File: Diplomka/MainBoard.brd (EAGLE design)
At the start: 100 x 80 mm, 6 parts, among them K1 ARK550/2, K2 ARK550/2, U1 ESP32-WROOM-32, U2 AMS1117-3.3

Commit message: Hotová první verze schématu
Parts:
- added LED1: (no value), led:CHIP-LED0805
- added Q1: AP2012P3C-P22, SamacSys_Parts:AP2012P3CP22
- added Q2: BC817-40LT1SMD, transistor-npn:SOT23-BEC
- added R1, R4: 1K, rcl:R0805
- added R10, R11, R12: 10k, rcl:R0805
- added R2: 1.5k, rcl:R0805
- added R3, R5: 2K, rcl:R0805
- added R6, R8: 1k, rcl:R0805
- added R7: 2k, rcl:R0805
- added R9: 150, rcl:R0805
- added SW1, SW2, SW3: TACTB-64K-F, #PaJa_prepinace:TACTB-64K-F
- added U$1: HC-SR501, Sensors_PIR_Lux:HC-SR501
- added U$2: MQ2, myParts:MQ2
- added U$3: GY4466, myParts:GY4466
- added U$4: BUZZER, myParts:BUZZER
- added U$5: HTU21D, myParts:HTU21D
- C1, C2: value 100n -> 100uF
- moved C2 88.7 mm to (-22.9, 72.4)
- moved C1 87.0 mm to (-16.5, 72.4)
- moved K1 60.1 mm to (-25.4, 64.8)
- moved K2 60.1 mm to (-34.3, 64.8)
- moved U2 31.7 mm to (-55.9, 39.4)
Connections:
- new net BTN_OUTPUT: R12.1, SW3.1, U1.13
- new net BUZZER_CONTROL: R8.1, U1.12
- new net I2C_SCL: U$5.SCL, U1.36
- new net I2C_SDA: U$5.SDA, U1.33
- new net LED_CONTROL: R9.2, U1.11
- new net MIC_OUT: U$3.OUT, U1.5
- new net MQ2_AO: R4.1, R5.2
- new net MQ2_DO: R1.1, R3.2
- new net N$1: Q2.C, U$4.-
- new net N$2: Q2.B, R8.2
- new net N$3: R1.2, U$2.DO
- new net N$4: R4.2, U$2.AO
- new net N$5: LED1.A, R9.1
- new net N$6: R6.2, U$1.OUT
- new net N$7: R10.1, SW1.3, U1.3
- new net N$8: R11.1, SW2.1, U1.25
- new net PHOTOTRAN: Q1.2, R2.2, U1.4
- new net PIR_DO: R6.1, R7.2, U1.24
- net 3V3: now also Q1.1, R10.2, R11.2, R12.2, U$3.VCC, U$5.VIN
- net 5V: now also K1.2, U$1.VCC, U$2.VCC, U$4.+; no longer K1.1
- net GND: now also K1.1, LED1.C, Q2.E, R2.1, R3.1, R5.1, R7.1, SW1.1, SW2.3, SW3.3, U$1.GND, U$2.GND, U$3.GND, U$5.GND; no longer K1.2

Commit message: Schema v1.0 hotovo
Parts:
- removed SW1, SW2, SW3: TACTB-64K-F, #PaJa_prepinace:TACTB-64K-F
- added U$6, U$7, U$8: TS6604B, myParts:TS6604B
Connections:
- new net N$9: R10.1
- net BTN_OUTPUT: now also U$8.+; no longer SW3.1
- net GND: now also U$6.-, U$7.-, U$8.-; no longer SW1.1, SW2.3, SW3.3
- net N$7: now also U$6.+; no longer R10.1, SW1.3
- net N$8: now also U$7.+; no longer SW2.1
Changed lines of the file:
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@@
 <attribute name="VALUE" x="-81.915" y="-44.45" size="1.27" layer="27"/>
-</element>
-<element name="SW1" library="#PaJa_prepinace" package="TACTB-64K-F" value="TACTB-64K-F" x="-2.8575" y="-115.285" smashed="yes">
-<attribute name="NAME" x="-5.2428" y="-113.6948" size="1.27" layer="25"/>
-<attribute name="VALUE" x="-5.2433" y="-118.147" size="1.27" layer="27"/>
 </element>
 <element name="R10" library="rcl" library_urn="urn:adsk.eagle:library:334" package="R0805" package3d_urn="urn:adsk.eagle:package:23553/2" value="10k" x="-81.28" y="-57.15" smashed="yes">
@@
 <attribute name="VALUE" x="-81.915" y="-66.04" size="1.27" layer="27"/>
 </element>
-<element name="SW2" library="#PaJa_prepinace" package="TACTB-64K-F" value="TACTB-64K-F" x="-2.8575" y="-131.795" smashed="yes">
-<attribute name="NAME" x="-5.2428" y="-130.2048" size="1.27" layer="25"/>
-<attribute name="VALUE" x="-5.2433" y="-134.657" size="1.27" layer="27"/>
-</element>
 <element name="R12" library="rcl" library_urn="urn:adsk.eagle:library:334" package="R0805" package3d_urn="urn:adsk.eagle:package:23553/2" value="10k" x="-81.28" y="-78.74" smashed="yes">
 <attribute name="NAME" x="-81.915" y="-77.47" size="1.27" layer="25"/>
@@
 <attribute name="VALUE" x="-81.915" y="-81.28" size="1.27" layer="27"/>
 </element>
-<element name="SW3" library="#PaJa_prepinace" package="TACTB-64K-F" value="TACTB-64K-F" x="-2.8575" y="-148.305" smashed="yes">
-<attribute name="NAME" x="-5.2428" y="-146.7148" size="1.27" layer="25"/>
-<attribute name="VALUE" x="-5.2433" y="-151.167" size="1.27" layer="27"/>
-</element>
 <element name="U$5" library="myParts" package="HTU21D" value="HTU21D" x="-83.82" y="-100.33" smashed="yes"/>
+<element name="U$6" library="myParts" package="TS6604B" value="TS6604B" x="-83.82" y="-157.48" smashed="yes"/>
+<element name="U$7" library="myParts" package="TS6604B" value="TS6604B" x="-83.82" y="-165.1" smashed="yes"/>
+<element name="U$8" library="myParts" package="TS6604B" value="TS6604B" x="-83.82" y="-172.72" smashed="yes"/>
 </elements>
 <signals>
@@
 <contactref element="LED1" pad="C"/>
 <contactref element="K1" pad="1"/>
-<contactref element="SW1" pad="1"/>
-<contactref element="SW2" pad="3"/>
-<contactref element="SW3" pad="3"/>
 <contactref element="U$5" pad="GND"/>
 <contactref element="R5" pad="1"/>
@@
 <contactref element="R7" pad="1"/>
 <contactref element="U$1" pad="GND"/>
+<contactref element="U$6" pad="-"/>
+<contactref element="U$7" pad="-"/>
+<contactref element="U$8" pad="-"/>
+<wire x1="-83.82" y1="-157.48" x2="-83.82" y2="-165.1" width="0" layer="19" extent="1-1"/>
+<wire x1="-83.82" y1="-172.72" x2="-83.82" y2="-165.1" width="0" layer="19" extent="1-1"/>
+<wire x1="-82.55" y1="-93.98" x2="-83.82" y2="-157.48" width="0" layer="19" extent="1-1"/>
 <wire x1="-81.28" y1="-34.51" x2="-82.55" y2="-93.98" width="0" layer="19" extent="1-1"/>
 <wire x1="-72.71" y1="-30.31" x2="-81.28" y2="-34.51" width="0" layer="19" extent="1-1"/>
@@
 <wire x1="-58.1" y1="62.23" x2="-44.13" y2="72.39" width="0" layer="19" extent="1-1"/>
 <wire x1="-59.225" y1="41.66" x2="-58.1" y2="62.23" width="0" layer="19" extent="1-1"/>
-<wire x1="-5.715" y1="-113.38" x2="-82.55" y2="-93.98" width="0" layer="19" extent="1-1"/>
-<wire x1="0" y1="-95.22" x2="-5.715" y2="-113.38" width="0" layer="19" extent="1-1"/>
-<wire x1="-5.715" y1="-133.7" x2="-5.715" y2="-113.38" width="0" layer="19" extent="1-1"/>
-<wire x1="-5.715" y1="-150.21" x2="-5.715" y2="-133.7" width="0" layer="19" extent="1-1"/>
+<wire x1="0" y1="-95.22" x2="-82.55" y2="-93.98" width="0" layer="19" extent="1-1"/>
 </signal>
 <signal name="5V">
@@
 </signal>
 <signal name="N$7">
-<contactref element="SW1" pad="3"/>
-<contactref element="R10" pad="1"/>
 <contactref element="U1" pad="3"/>
-<wire x1="-31.36" y1="19.23" x2="-82.23" y2="-57.15" width="0" layer="19" extent="1-1"/>
-<wire x1="-5.715" y1="-117.19" x2="-82.23" y2="-57.15" width="0" layer="19" extent="1-1"/>
+<contactref element="U$6" pad="+"/>
+<wire x1="-31.36" y1="19.23" x2="-83.82" y2="-152.98" width="0" layer="19" extent="1-1"/>
 </signal>
 <signal name="N$8">
 <contactref element="R11" pad="1"/>
 <contactref element="U1" pad="25"/>
-<contactref element="SW2" pad="1"/>
+<contactref element="U$7" pad="+"/>
+<wire x1="-82.23" y1="-63.5" x2="-83.82" y2="-160.6" width="0" layer="19" extent="1-1"/>
 <wire x1="-14.36" y1="5.26" x2="-82.23" y2="-63.5" width="0" layer="19" extent="1-1"/>
-<wire x1="-5.715" y1="-129.89" x2="-82.23" y2="-63.5" width="0" layer="19" extent="1-1"/>
 </signal>
 <signal name="BTN_OUTPUT">
-<contactref element="SW3" pad="1"/>
 <contactref element="R12" pad="1"/>
 <contactref element="U1" pad="13"/>
+<contactref element="U$8" pad="+"/>
+<wire x1="-82.23" y1="-78.74" x2="-83.82" y2="-168.22" width="0" layer="19" extent="1-1"/>
 <wire x1="-31.36" y1="6.53" x2="-82.23" y2="-78.74" width="0" layer="19" extent="1-1"/>
-<wire x1="-5.715" y1="-146.4" x2="-82.23" y2="-78.74" width="0" layer="19" extent="1-1"/>
+</signal>
+<signal name="N$9">
+<contactref element="R10" pad="1"/>
 </signal>
 </signals>

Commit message: Nektere soucastky nyni budou napajene z ESP32. Pridan soubor co obsahuje kosik v GME.
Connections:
- new net N$10: U1.23
- new net PHOTOTRAN_CONTROL: Q1.1, U1.6
- net 3V3: no longer Q1.1
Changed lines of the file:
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@@
 <drawing>
 <settings>
-<setting alwaysvectorfont="no"/>
+<setting alwaysvectorfont="yes"/>
 <setting verticaltext="up"/>
 </settings>
@@
 <contactref element="C2" pad="1"/>
 <contactref element="U1" pad="2"/>
-<contactref element="Q1" pad="1"/>
 <contactref element="U$3" pad="VCC"/>
 <contactref element="R10" pad="2"/>
@@
 <wire x1="-31.36" y1="20.5" x2="-66.548" y2="-9.906" width="0" layer="19" extent="1-1"/>
 <wire x1="-59.225" y1="39.37" x2="-31.36" y2="20.5" width="0" layer="19" extent="1-1"/>
-<wire x1="-54.515" y1="69.85" x2="-59.225" y2="39.37" width="0" layer="19" extent="1-1"/>
-<wire x1="-23.81" y1="72.39" x2="-54.515" y2="69.85" width="0" layer="19" extent="1-1"/>
+<wire x1="-23.81" y1="72.39" x2="-59.225" y2="39.37" width="0" layer="19" extent="1-1"/>
 </signal>
 <signal name="PHOTOTRAN">
@@
 <contactref element="R10" pad="1"/>
 </signal>
+<signal name="N$10">
+<contactref element="U1" pad="23"/>
+</signal>
+<signal name="PHOTOTRAN_CONTROL">
+<contactref element="U1" pad="6"/>
+<contactref element="Q1" pad="1"/>
+<wire x1="-54.515" y1="69.85" x2="-31.36" y2="15.42" width="0" layer="19" extent="1-1"/>
+</signal>
 </signals>

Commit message: Zmeny v PCB
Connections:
- removed net N$10: U1.23
- new net MIC_CONTROL: U$3.OUT, U1.23
- new net TEMP_CONTROL: U$5.VIN, U1.28
- net 3V3: no longer U$5.VIN
- net MIC_OUT: no longer U$3.OUT
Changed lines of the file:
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@@
 <contactref element="R11" pad="2"/>
 <contactref element="R12" pad="2"/>
-<contactref element="U$5" pad="VIN"/>
-<wire x1="-80.33" y1="-78.74" x2="-82.55" y2="-91.44" width="0" layer="19" extent="1-1"/>
 <wire x1="-80.33" y1="-63.5" x2="-80.33" y2="-78.74" width="0" layer="19" extent="1-1"/>
 <wire x1="-80.33" y1="-57.15" x2="-80.33" y2="-63.5" width="0" layer="19" extent="1-1"/>
@@
 </signal>
 <signal name="MIC_OUT">
-<contactref element="U$3" pad="OUT"/>
 <contactref element="U1" pad="5"/>
-<wire x1="-31.36" y1="16.69" x2="-71.628" y2="-9.906" width="0" layer="19" extent="1-1"/>
 </signal>
 <signal name="N$1">
@@
 <contactref element="R10" pad="1"/>
 </signal>
-<signal name="N$10">
+<signal name="MIC_CONTROL">
 <contactref element="U1" pad="23"/>
+<contactref element="U$3" pad="OUT"/>
+<wire x1="-18.415" y1="4.26" x2="-71.628" y2="-9.906" width="0" layer="19" extent="1-1"/>
 </signal>
 <signal name="PHOTOTRAN_CONTROL">
@@
 <wire x1="-54.515" y1="69.85" x2="-31.36" y2="15.42" width="0" layer="19" extent="1-1"/>
 </signal>
+<signal name="TEMP_CONTROL">
+<contactref element="U1" pad="28"/>
+<contactref element="U$5" pad="VIN"/>
+<wire x1="-14.36" y1="9.07" x2="-82.55" y2="-91.44" width="0" layer="19" extent="1-1"/>
+</signal>
 </signals>

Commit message: Přidány do repozitáře pravidla JLCPCB, nakresleno PCB asi z 70%ˇ.
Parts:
- added C3, C4: 100nF, rcl:C0805
- C1, C2: value 100uF -> 10uF
- moved U$7 246.0 mm to (61.2, 33.6)
- moved U$6 241.8 mm to (29.5, 56.1)
- moved U$8 221.0 mm to (31.0, 16.1)
- moved U$5 215.9 mm to (73.1, 47.9)
- moved U$2 179.3 mm to (36.8, 69.0)
- moved R11 170.0 mm to (58.5, 33.3), turned to 270 degrees
- moved R10 166.1 mm to (32.9, 63.5), turned to 180 degrees
- moved U$3 159.5 mm to (73.0, 44.9), turned to 270 degrees
- moved R9 156.7 mm to (61.5, 22.6), turned to 90 degrees
- moved R12 155.5 mm to (31.5, 28.3), turned to 90 degrees
- moved LED1 152.5 mm to (61.5, 18.0), turned to 180 degrees
- moved Q2 138.2 mm to (51.4, 29.6), turned to 180 degrees
- moved R8 136.6 mm to (44.0, 30.4), turned to 270 degrees
- moved U$4 127.6 mm to (51.0, 18.0)
- moved K2 121.7 mm to (87.0, 75.4), turned to 135 degrees
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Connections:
- removed net N$9: R10.1
- net 3V3: now also C4.1; no longer U$3.VCC
- net 5V: now also C3.1
- net BTN_OUTPUT: now also U1.11; no longer U1.13
- net GND: now also C3.2, C4.2
- net LED_CONTROL: now also U1.16; no longer U1.11
- net MIC_CONTROL: now also U$3.VCC, U1.26; no longer U$3.OUT, U1.23
- net MIC_OUT: now also U$3.OUT
- net MQ2_AO: now also U1.4
- net MQ2_DO: now also U1.37
- net N$7: now also R10.1
- net PHOTOTRAN: now also U1.8; no longer U1.4
- net PHOTOTRAN_CONTROL: now also U1.7; no longer U1.6
- net PIR_DO: now also U1.6; no longer U1.24
- net TEMP_CONTROL: now also U1.31; no longer U1.28
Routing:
- net 3V3: track 0.00 -> 156.4 mm, vias 0 -> 2
- net 5V: track 0.00 -> 119.0 mm
- net MIC_OUT: track 0.00 -> 56.9 mm, vias 0 -> 1
- net RXD0: track 0.00 -> 42.5 mm, vias 0 -> 1
- net TXD0: track 0.00 -> 41.8 mm, vias 0 -> 1
- net BTN_OUTPUT: track 0.00 -> 30.6 mm
- net TEMP_CONTROL: track 0.00 -> 29.6 mm
- net N$3: track 0.00 -> 27.6 mm
- net N$7: track 0.00 -> 23.7 mm
- net MQ2_AO: track 0.00 -> 22.4 mm, vias 0 -> 1
- net LED_CONTROL: track 0.00 -> 21.6 mm
- net MQ2_DO: track 0.00 -> 20.8 mm
- net MIC_CONTROL: track 0.00 -> 18.0 mm
- net PHOTOTRAN: track 0.00 -> 17.3 mm
- net I2C_SCL: track 0.00 -> 16.4 mm
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- added copper zone on layer 1, net GND
- added copper zone on layer 16, net GND
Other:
- board size 100 x 80 mm -> 100 x 100 mm

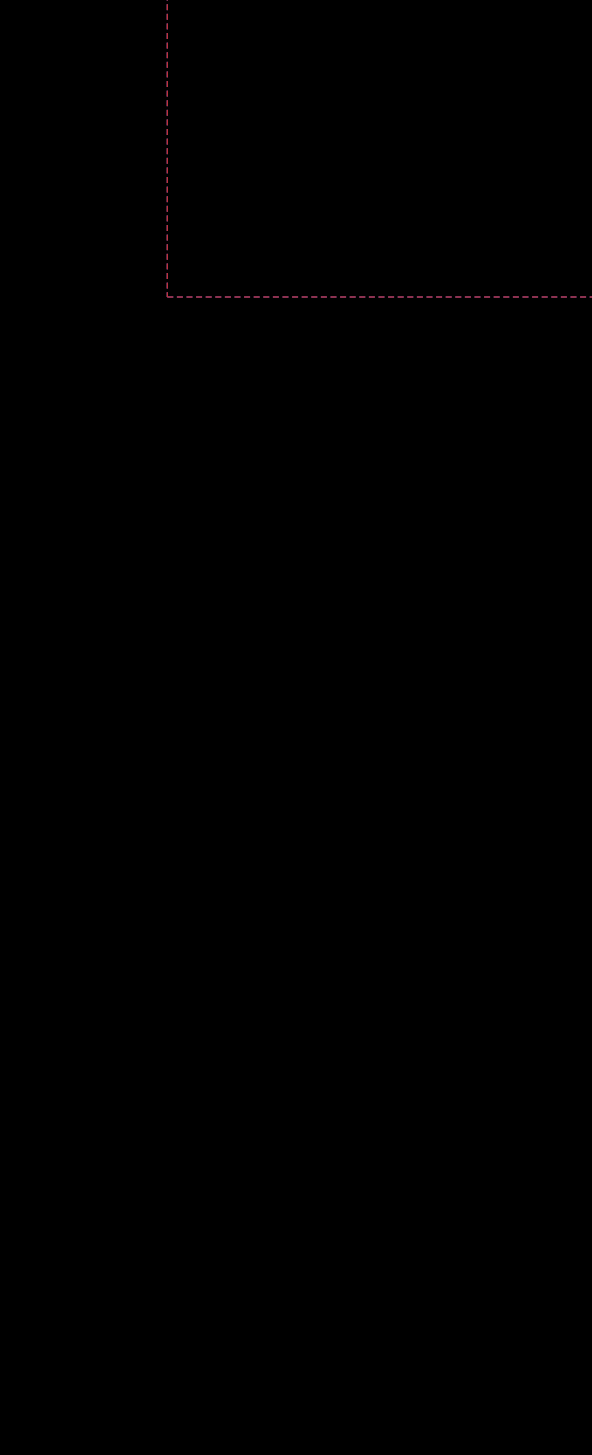
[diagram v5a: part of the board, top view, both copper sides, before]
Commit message: Přidán stepdown converted. Třeba dodat vhodnou cívku a dokreslit desku.
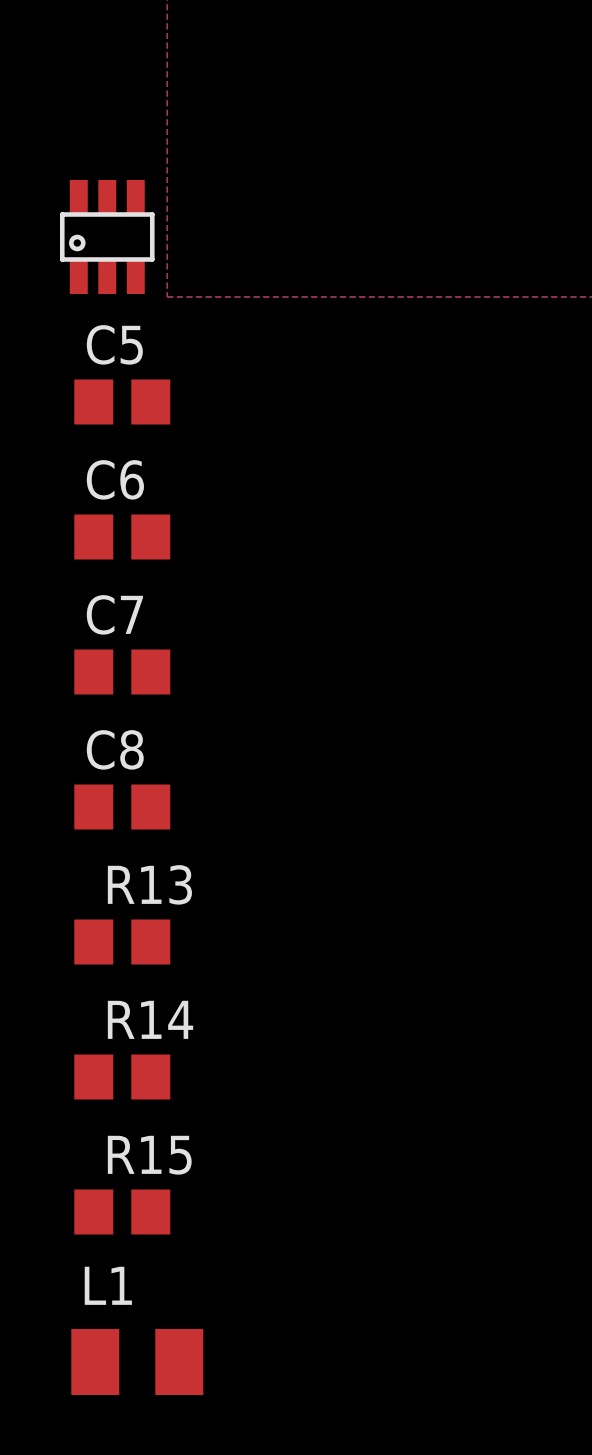
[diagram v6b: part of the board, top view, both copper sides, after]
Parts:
- added C5: 22n, rcl:C0805
- added C6, C7: 22u, rcl:C0805
- added C8: 10u, rcl:C0805
- added L1: (no value), rcl:L3225M
- added R13: 110k, rcl:R0805
- added R14: 15k, rcl:R0805
- added R15: 100k, rcl:R0805
- added U$9: SD8942, myParts:SD8942
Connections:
- new net N$10: C5.2, L1.1, U$9.SW
- new net N$11: R15.1, U$9.EN
- new net N$12: R13.1, R14.2, U$9.FB
- new net N$9: C5.1, U$9.BS
- new net VIN: C8.1, R15.2, U$9.IN
- new net VOUT: C6.1, C7.1, L1.2, R13.2
- net GND: now also C6.2, C7.2, C8.2, R14.1, U$9.GND

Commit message: Cca hotový plošňák, třeba udělat nějaké úpravy ale jinak dobré.
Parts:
- removed K2: ARK550/2, #PaJa_konektory:ARK550/2
- added JUM1: S1G6_JUMP, #PaJa_konektory:S1G6_JUM
- added Q3, Q4: SS8050-G, SS8050-G:SOT95P240X115-3N
- added R16, R17: (no value), rcl:R0805
- C8: value 10u -> 10u/25V
- L1: value (none) -> SRR1260-4R7Y; device rcl:L3225M -> SRR1260-4R7Y:SRR12604R7Y
- moved L1 137.6 mm to (51.1, 91.8), flipped to the bottom
- moved R15 126.7 mm to (31.0, 92.0), flipped to the bottom
- moved C8 117.6 mm to (36.0, 94.5), flipped to the bottom, turned to 180 degrees
- moved R14 117.4 mm to (32.0, 86.5), flipped to the bottom, turned to 135 degrees
- moved R13 115.0 mm to (36.5, 87.0), flipped to the bottom, turned to 180 degrees
- moved C7 110.0 mm to (42.0, 88.5), flipped to the bottom
- moved C6 108.1 mm to (42.0, 91.0), flipped to the bottom
- moved C5 102.2 mm to (38.5, 90.5), flipped to the bottom, turned to 90 degrees
- moved U$9 95.9 mm to (35.0, 90.5), flipped to the bottom
- moved C3 6.28 mm to (20.5, 73.6)
- moved C2 1.90 mm to (22.6, 70.0), turned to 270 degrees
- moved C1 1.36 mm to (20.5, 77.1)
- moved R6 1.00 mm to (32.5, 48.2)
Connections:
- removed net N$7: R10.1, U$6.+, U1.3
- removed net N$8: R11.1, U$7.+, U1.25
- removed net RXD0: K2.1, U1.34
- removed net TXD0: K2.2, U1.35
- removed net VOUT: C6.1, C7.1, L1.2, R13.2
- new net CTS: JUM1.5, Q4.1, R17.2
- new net DTR: JUM1.1, Q4.2, R16.1
- new net EN: Q3.3, R10.1, U$6.+, U1.3
- new net IO0: Q4.3, R11.1, U$7.+, U1.25
- new net N$13: Q3.1, R16.2
- new net N$15: Q3.2, R17.1
- new net UART_PC_RX: JUM1.2, U1.35
- new net UART_PC_TX: JUM1.3, U1.34
- new net VCC: JUM1.4
- net 5V: now also C6.1, C7.1, L1.2, R13.2; no longer K1.2
- net GND: now also JUM1.6
- net VIN: now also K1.2
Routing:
- net DTR: track 0.00 -> 118.4 mm, vias 0 -> 2
- net CTS: track 0.00 -> 64.2 mm
- net N$15: track 0.00 -> 55.9 mm, vias 0 -> 2
- net RXD0: track 42.5 -> 0.00 mm, vias 1 -> 0
- net TXD0: track 41.8 -> 0.00 mm, vias 1 -> 0
- net UART_PC_TX: track 0.00 -> 39.8 mm, vias 0 -> 2
- net UART_PC_RX: track 0.00 -> 36.4 mm, vias 0 -> 2
- net EN: track 0.00 -> 26.5 mm
- net N$10: track 0.00 -> 24.7 mm
- net N$7: track 23.7 -> 0.00 mm
- net VIN: track 0.00 -> 19.0 mm
- net 3V3: track 156.4 -> 139.2 mm
- net 5V: track 119.0 -> 134.8 mm
- net IO0: track 0.00 -> 15.3 mm
- net GND: track 13.0 -> 0.00 mm, vias 1 -> 2
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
